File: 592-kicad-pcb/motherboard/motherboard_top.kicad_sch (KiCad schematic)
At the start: 12 parts, among them J17 Conn_02x01, J18 Conn_02x01, U14 74CBTLV3257, U15 74CBTLV3257

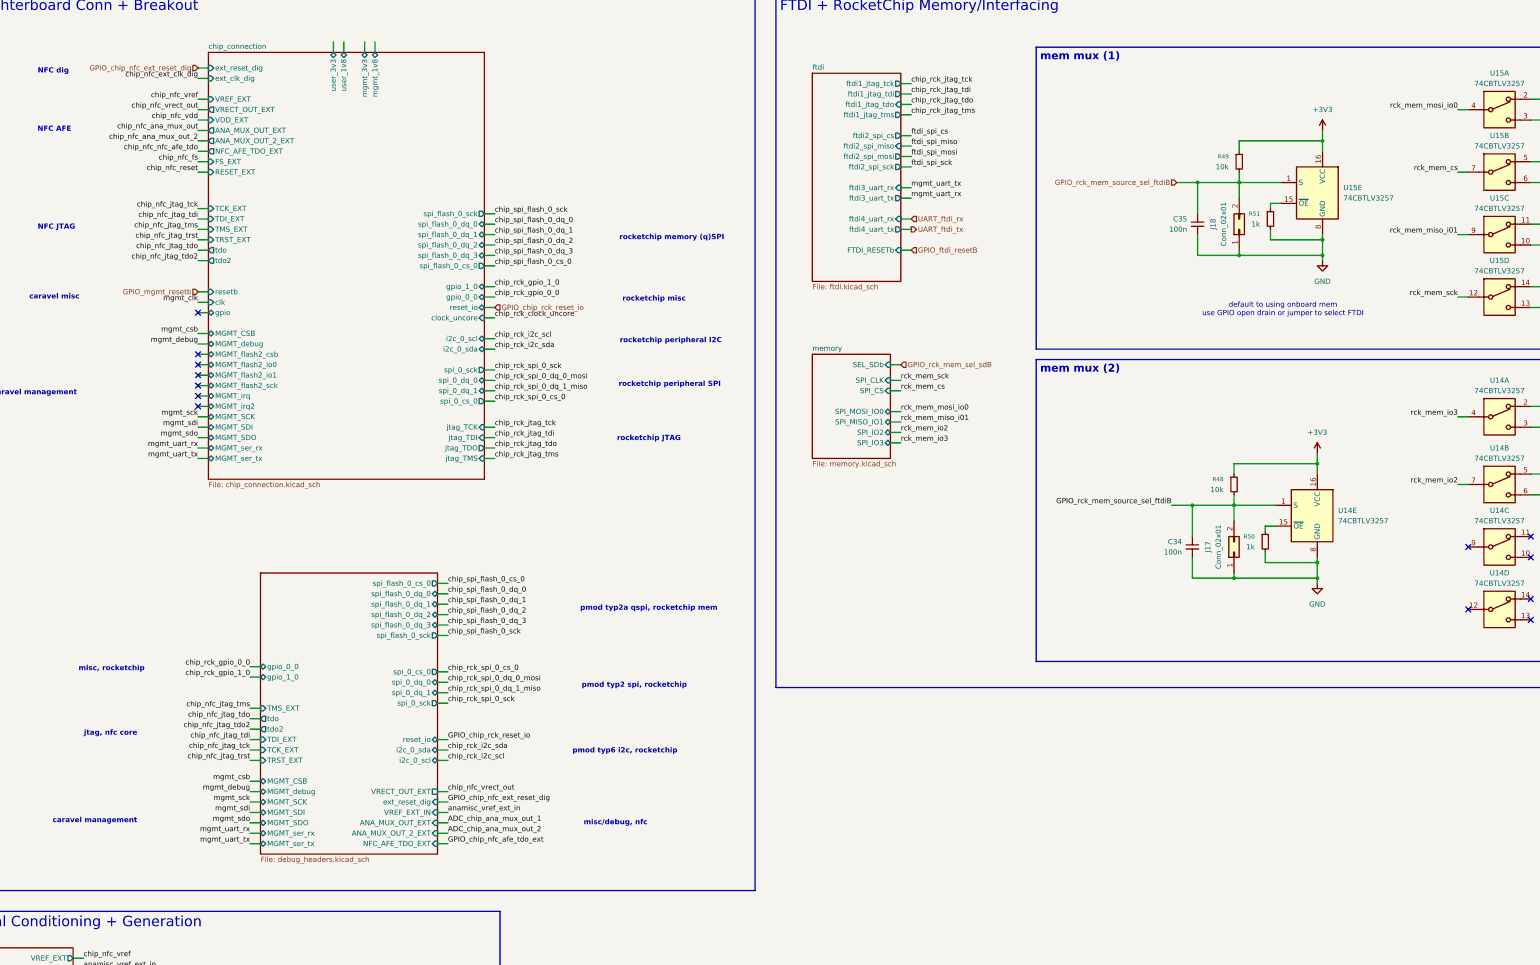
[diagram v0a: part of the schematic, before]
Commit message: partial update to use STM board, updated muxing of FTDI
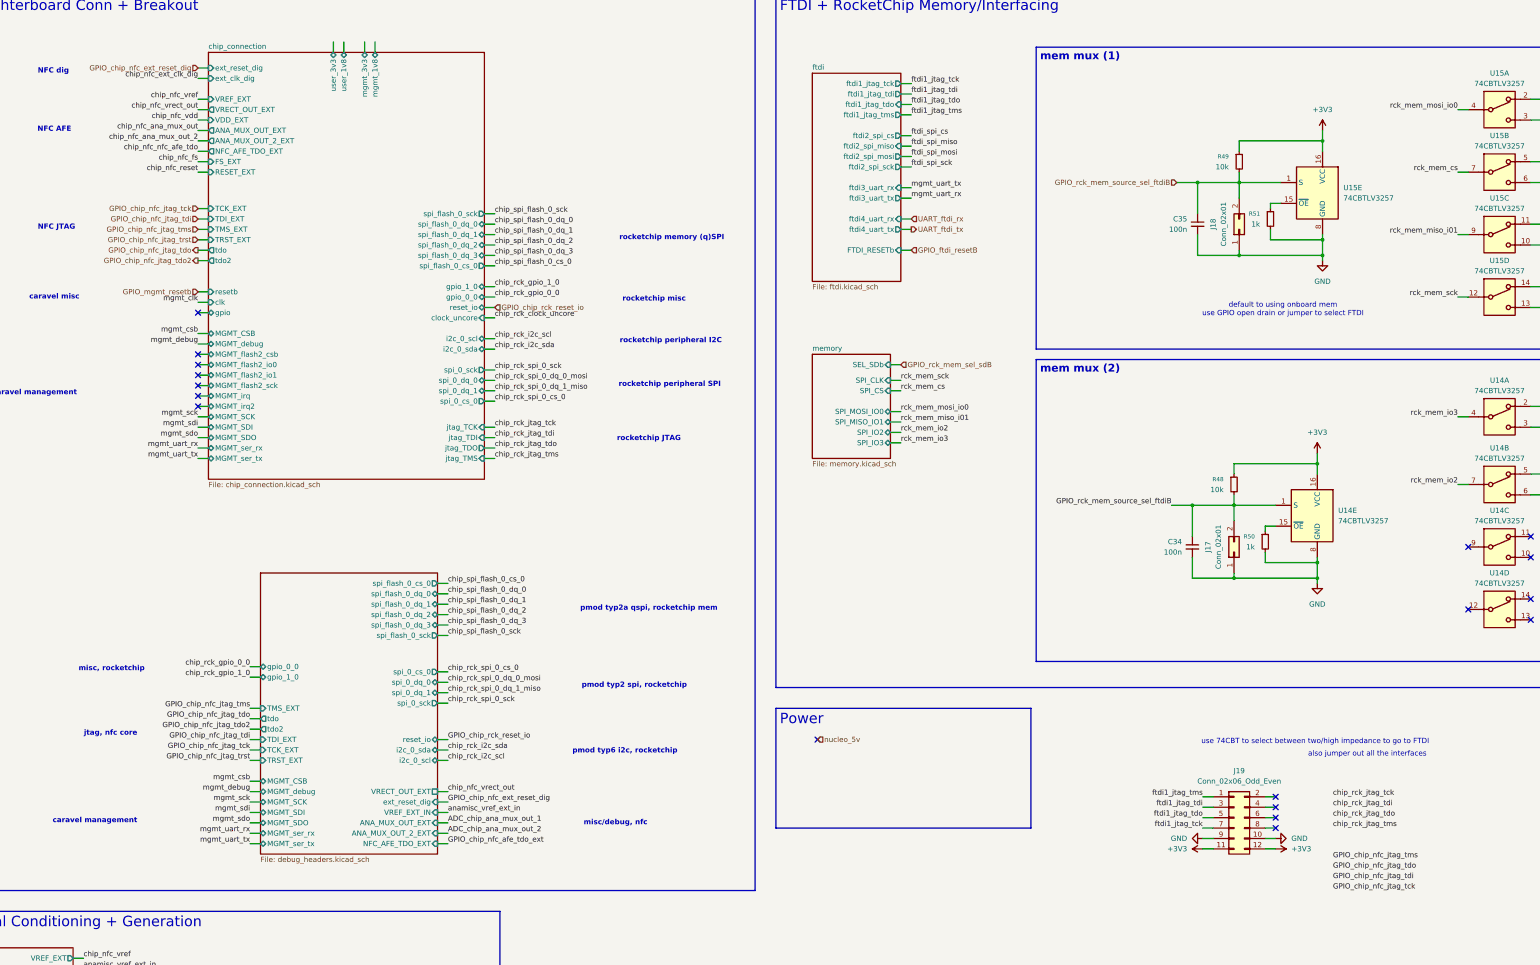
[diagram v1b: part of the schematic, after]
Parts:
- added J19: Conn_02x06_Odd_Even, Connector_PinSocket_2.54mm:PinSocket_2x06_P2.54mm_Horizontal, symbol Connector_Generic:Conn_02x06_Odd_Even
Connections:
- net +3V3: now also J19.11 (Pin_11), J19.12 (Pin_12)
- net GND: now also J19.10 (Pin_10), J19.9 (Pin_9)
- new net ftdi1_jtag_tck: J19.7 (Pin_7)
- new net ftdi1_jtag_tdi: J19.3 (Pin_3)
- new net ftdi1_jtag_tdo: J19.5 (Pin_5)
- new net ftdi1_jtag_tms: J19.1 (Pin_1)
- no-connect marks 13 -> 18
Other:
- note added: "also jumper out all the interfaces"
- note added: "use 74CBT to select between two/high impedance to go to FTDI"

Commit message: update FTDI interfacing
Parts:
- removed J19: Conn_02x06_Odd_Even, Connector_PinSocket_2.54mm:PinSocket_2x06_P2.54mm_Horizontal, symbol Connector_Generic:Conn_02x06_Odd_Even
- removed R50: 1k, symbol Device:R_Small
- added C36, C38: 100n, symbol Device:C_Small
- added J21, J22: Conn_02x01, symbol Connector_Generic:Conn_02x01
- added R56: 10k, symbol Device:R_Small
- added U17: 74CBTLV3257, symbol 74xx:74CBTLV3257
- added U18, U19: SN74LVC1G14DBV, Package_TO_SOT_SMD:SOT-23-5, symbol 74xGxx:SN74LVC1G14DBV
- R51: value 1k -> 10k
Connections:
- net +3V3: now also R51.1, R56.1, U17.16 (VCC), U18.5 (VCC), U19.5 (VCC)
- net GND: now also C36.2, C38.2, J21.1 (Pin_1), J22.1 (Pin_1), U17.8 (GND), U18.3 (GND), U19.3 (GND); no longer R51.2
- net GPIO_chip_nfc_jtag_tdo: now also U17.10
- net GPIO_rck_mem_source_sel_ftdiB: no longer C34.1, J17.2 (Pin_2), R48.2
- net chip_rck_jtag_tck: now also U17.14
- net chip_rck_jtag_tdi: now also U17.5
- net chip_rck_jtag_tdo: now also U17.11
- net chip_rck_jtag_tms: now also U17.2
- net ftdi1_jtag_tck: now also U17.12
- net ftdi1_jtag_tdi: now also U17.7
- net ftdi1_jtag_tdo: now also U17.9
- net ftdi1_jtag_tms: now also U17.4
- net rck_mem_source_enB: now reaches U14.15 (~{OE})
- net rck_mem_source_enB: now also U15.15 (~{OE}), U18.4
- new net GPIO_JTAG_FTDI_source_select: C34.1, J17.2 (Pin_2), R48.2, U17.1 (S)
- new net GPIO_ftdi_jtag_src_en: C36.1, J21.2 (Pin_2), R51.2, U19.2
- new net GPIO_rck_mem_source_en: C38.1, J22.2 (Pin_2), R56.2, U18.2
- new net chip_nfc_jtag_tck: U17.13
- new net chip_nfc_jtag_tdi: U17.6
- new net chip_nfc_jtag_tms: U17.3
- new net ftdi_jtag_src_enB: U17.15 (~{OE}), U19.4
- no-connect marks 18 -> 14
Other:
- sheet debug_headers ports: added rck_jtag_tck, rck_jtag_tdi, rck_jtag_tdo, rck_jtag_tms; removed none
- note added: "jtag, rocketchip"
- note removed: "also jumper out all the interfaces"
- note removed: "use 74CBT to select between two/high impedance to go to FTDI"
- moved on the sheet: C35, J18, R49, U15A, U15B, U15C, U15D, U15E

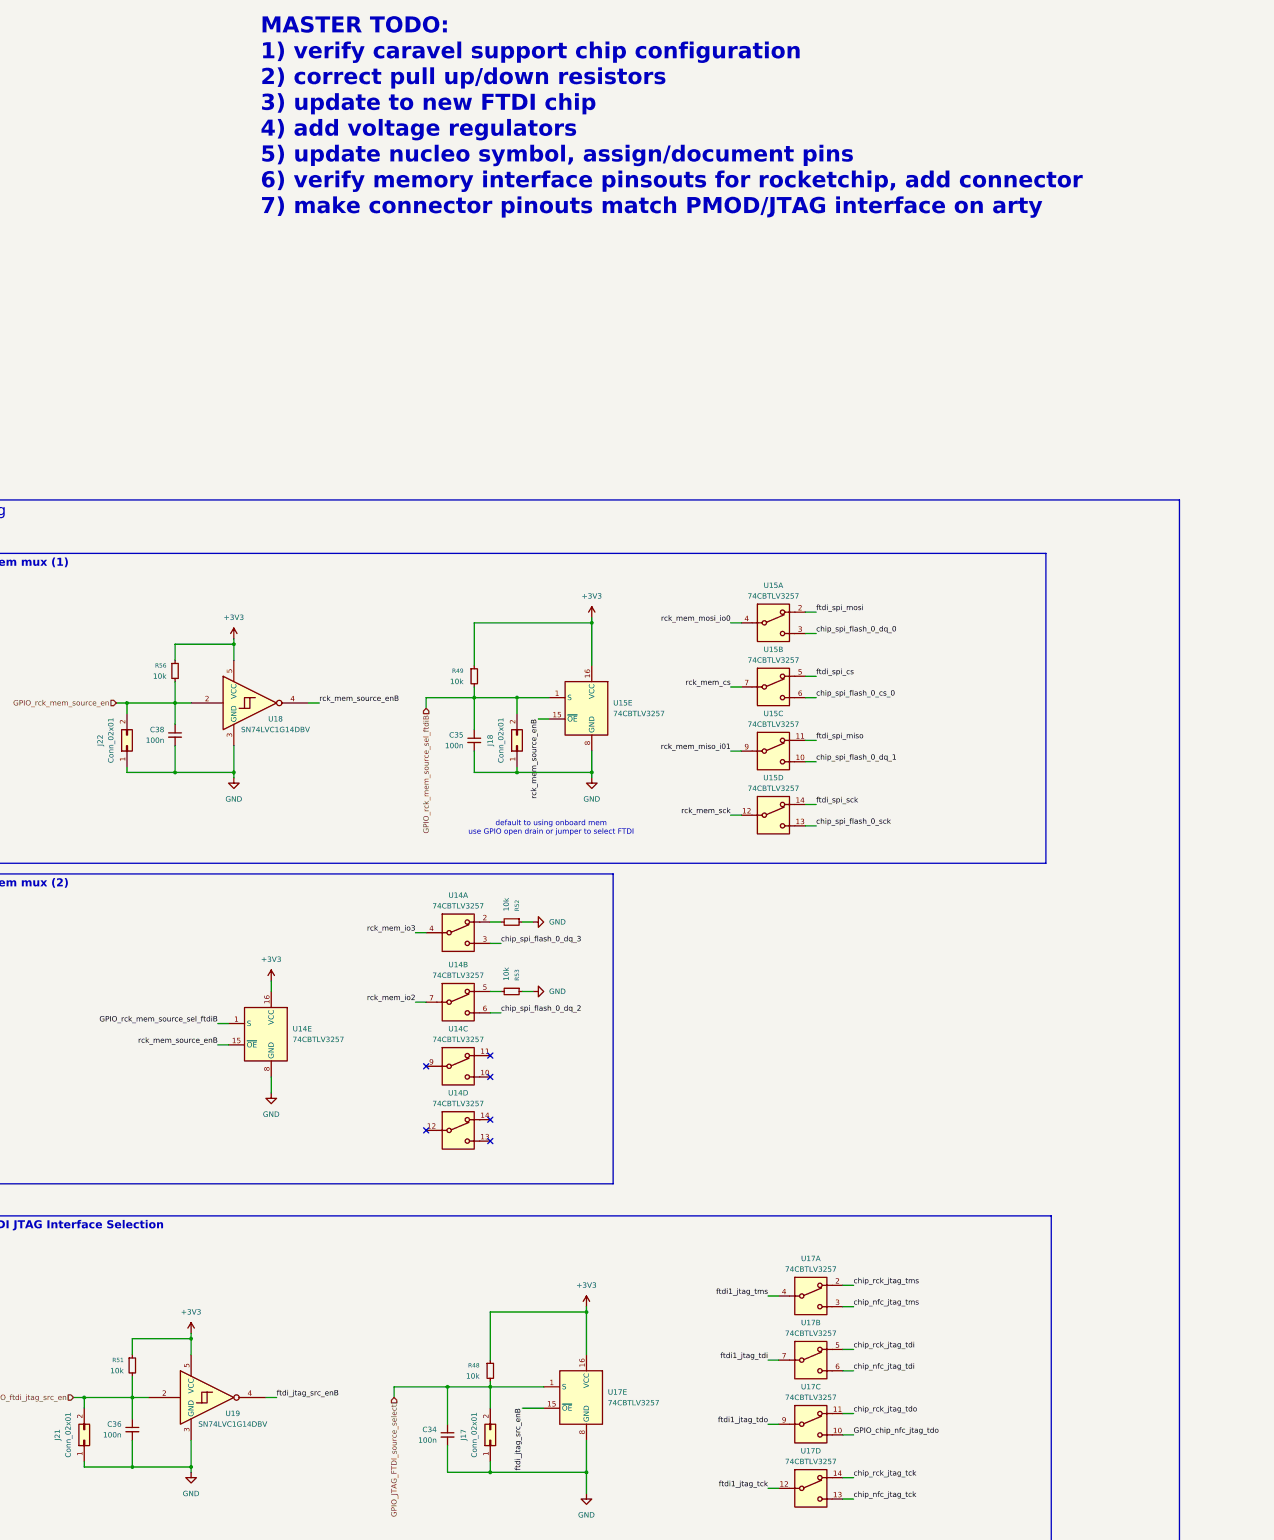
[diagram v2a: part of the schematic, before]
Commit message: add JLC part num for parts, footprints
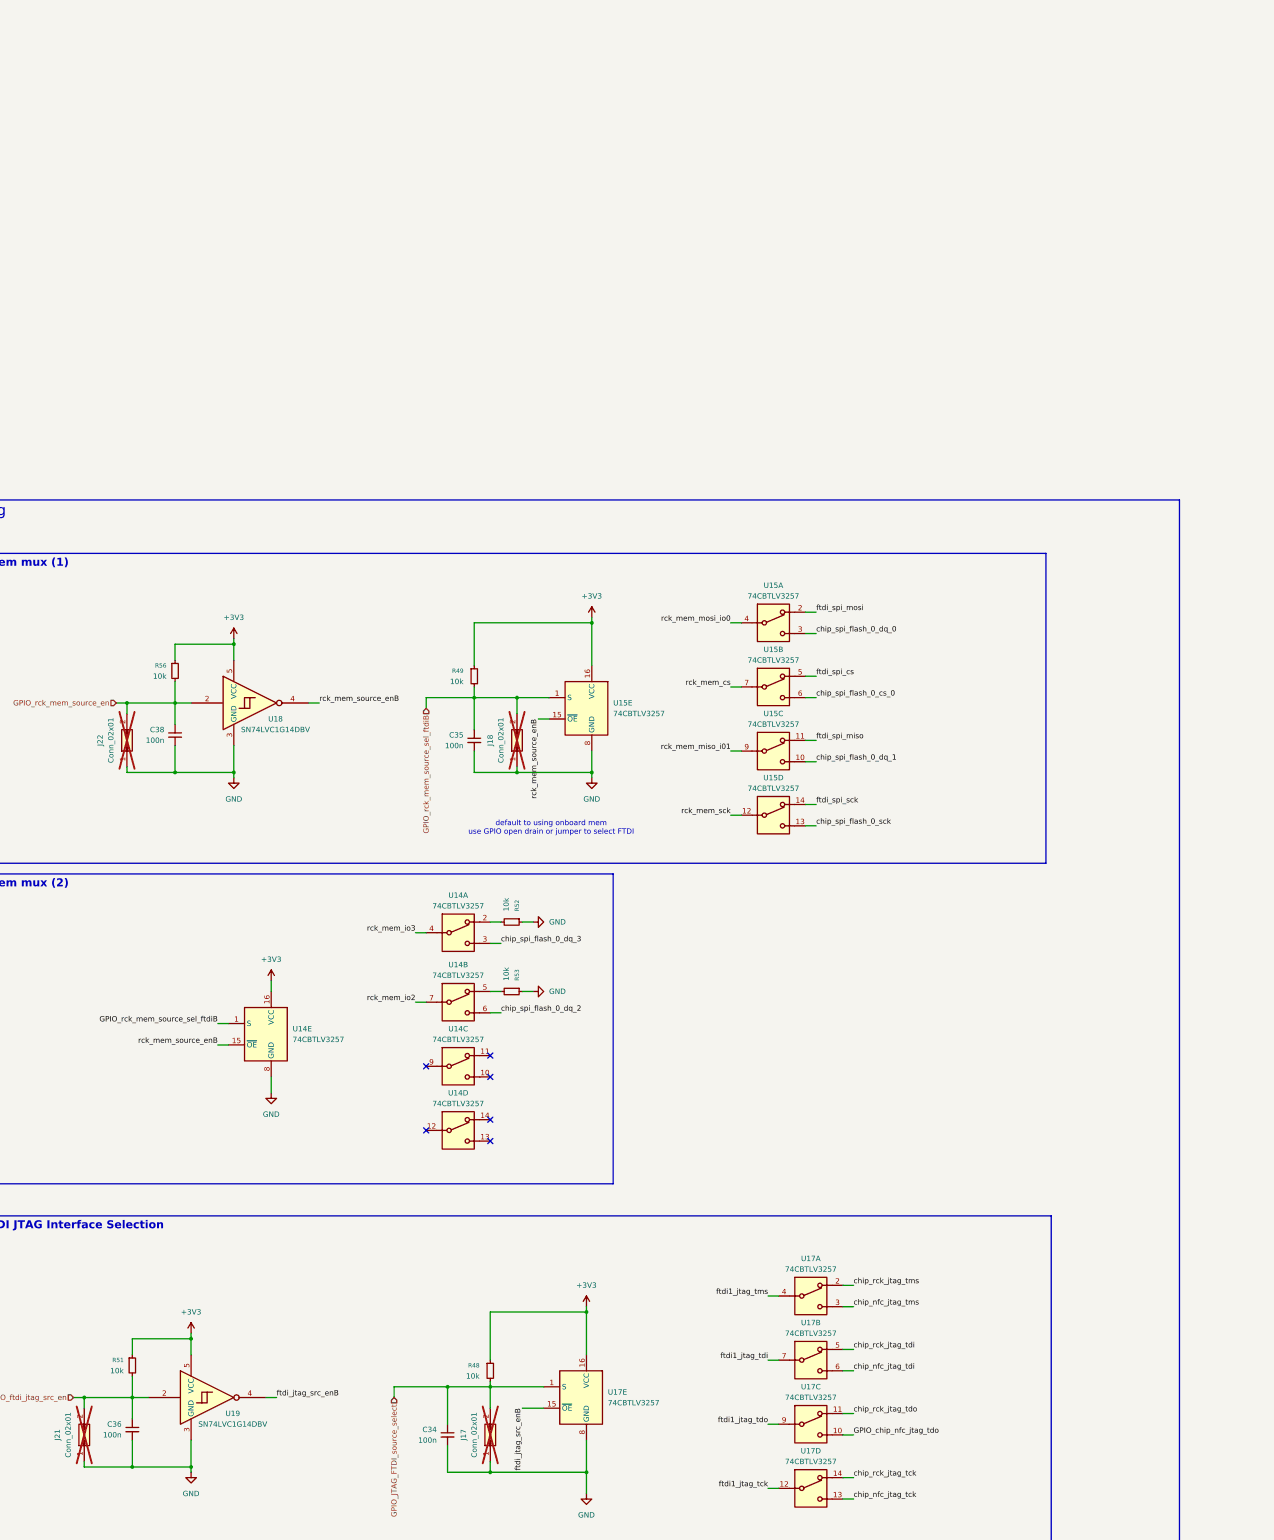
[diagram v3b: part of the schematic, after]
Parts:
- C34, C35, C36, C38: footprint (none) -> Capacitor_SMD:C_0402_1005Metric; LCSC (none) -> C1525
- J17, J18, J21, J22: footprint (none) -> Connector_PinHeader_1.27mm:PinHeader_1x02_P1.27mm_Vertical; now not fitted
- R48, R49, R51, R52, R53, R56: footprint (none) -> Resistor_SMD:R_0402_1005Metric; LCSC (none) -> C25744
- U14, U15, U17: footprint (none) -> Package_SO:SOIC-16W_5.3x10.2mm_P1.27mm; LCSC (none) -> C10012
- U18, U19: footprint Package_TO_SOT_SMD:SOT-23-5 -> Package_TO_SOT_SMD:SOT-353_SC-70-5; LCSC (none) -> C35740
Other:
- note removed: "MASTER TODO: 1) verify caravel support chip configuration 2) correct pull up/down resistors 3) update to new FTDI chip 4) add voltage regulators 5) update nucleo symbol, assign/document pins 6) verify memory interface pinsouts for rocketchip, add connector 7) make connector pinouts match PMOD/JTAG interface on arty"

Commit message: update footprints, final
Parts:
- U14, U15, U17: footprint Package_SO:SOIC-16W_5.3x10.2mm_P1.27mm -> Package_SO:SOIC-16_3.9x9.9mm_P1.27mm
